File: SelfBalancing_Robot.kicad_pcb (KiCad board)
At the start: 2 copper layers, 58.4 x 53.3 mm, 10 parts, among them P1 CONN_01X08, P2 CONN_01X06, P3 CONN_01X02, P4 CONN_01X02, P5 CONN_01X02, U1 ArduinoNano, U2 L293D

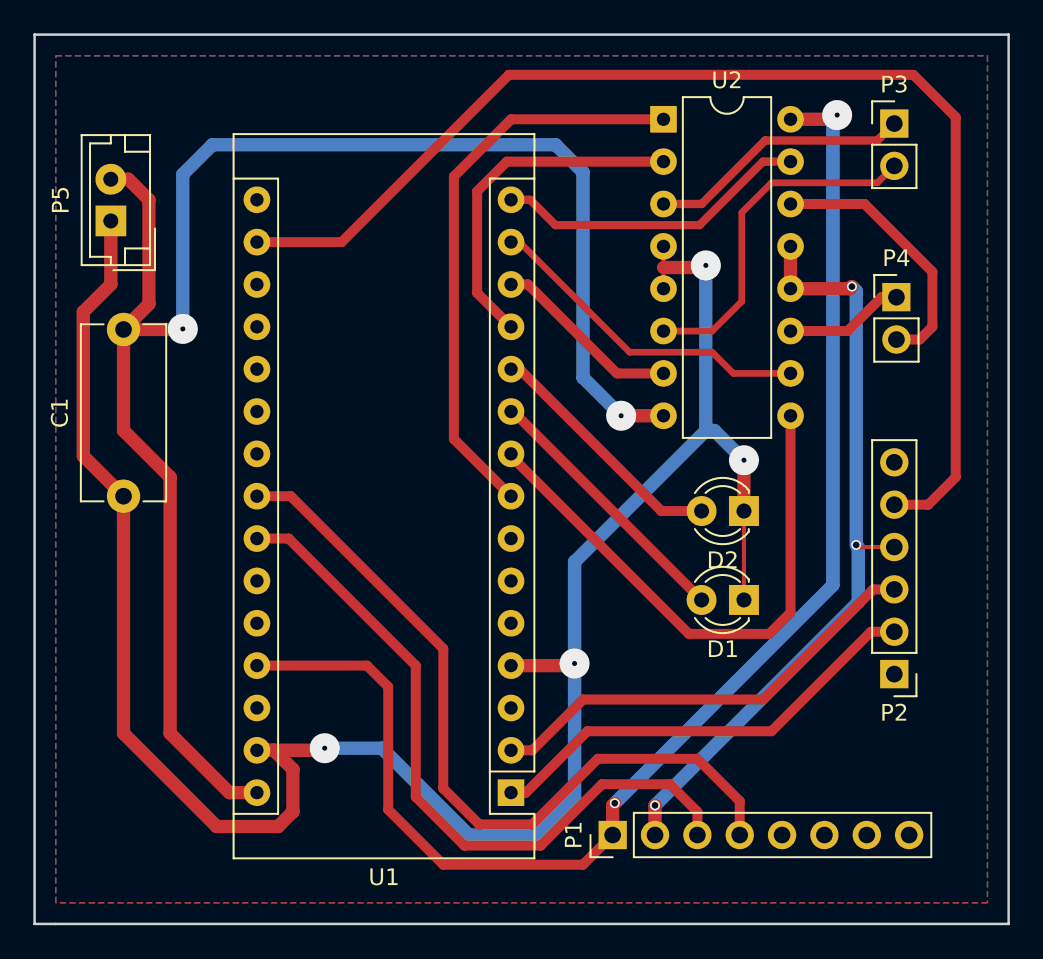
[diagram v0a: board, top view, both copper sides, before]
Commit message: +LED indicator resistors
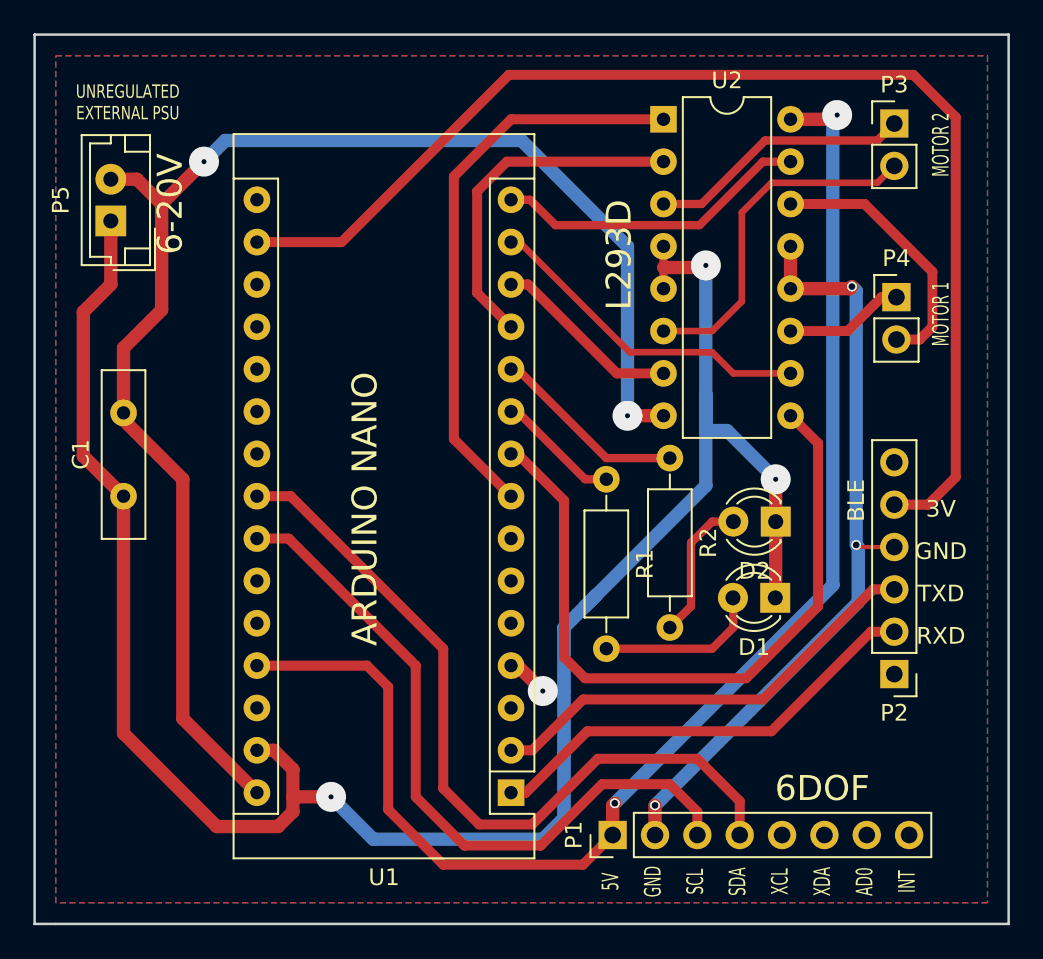
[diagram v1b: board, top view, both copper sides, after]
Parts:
- added R1: R, Resistors_ThroughHole:R_Axial_DIN0207_L6.3mm_D2.5mm_P10.16mm_Horizontal, F.Cu at (148.6, 97.8)
- added R2: R, Resistors_ThroughHole:R_Axial_DIN0207_L6.3mm_D2.5mm_P10.16mm_Horizontal, F.Cu at (152.4, 96.5)
- C1: footprint Capacitors_THT:C_Disc_D10.5mm_W5.0mm_P10.00mm -> Capacitors_THT:C_Disc_D10.0mm_W2.5mm_P5.00mm
- moved D2 2.01 mm to (158.8, 100.3)
- moved D1 1.88 mm to (158.7, 104.9)
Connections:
- U1 pad 10: Net-(D1-Pad2) -> Net-(R1-Pad1)
- U1 pad 11: Net-(D2-Pad2) -> Net-(R2-Pad1)
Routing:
- net Net-(R2-Pad1): track 0.00 -> 12.2 mm
- net /9V: track 99.6 -> 87.7 mm
- net /EN2: track 33.6 -> 43.5 mm
- net Net-(R1-Pad1): track 0.00 -> 7.53 mm
- net Net-(D1-Pad2): track 16.1 -> 9.42 mm
- net Net-(D2-Pad2): track 15.0 -> 8.67 mm
- net Net-(C1-Pad1): track 128.2 -> 132.0 mm
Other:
- board text added: "3V"
- board text added: "5V"
- board text added: "6-20V"
- board text added: "6DOF"
- board text added: "AD0"
- board text added: "ARDUINO NANO"
- board text added: "BLE"
- board text added: "GND"
- board text added: "INT"
- board text added: "L293D"
- board text added: "MOTOR 1"
- board text added: "MOTOR 2"
- board text added: "RXD"
- board text added: "SCL"
- board text added: "SDA"
- board text added: "TXD"
- board text added: "UNREGULATED EXTERNAL PSU"
- board text added: "XCL"
- board text added: "XDA"

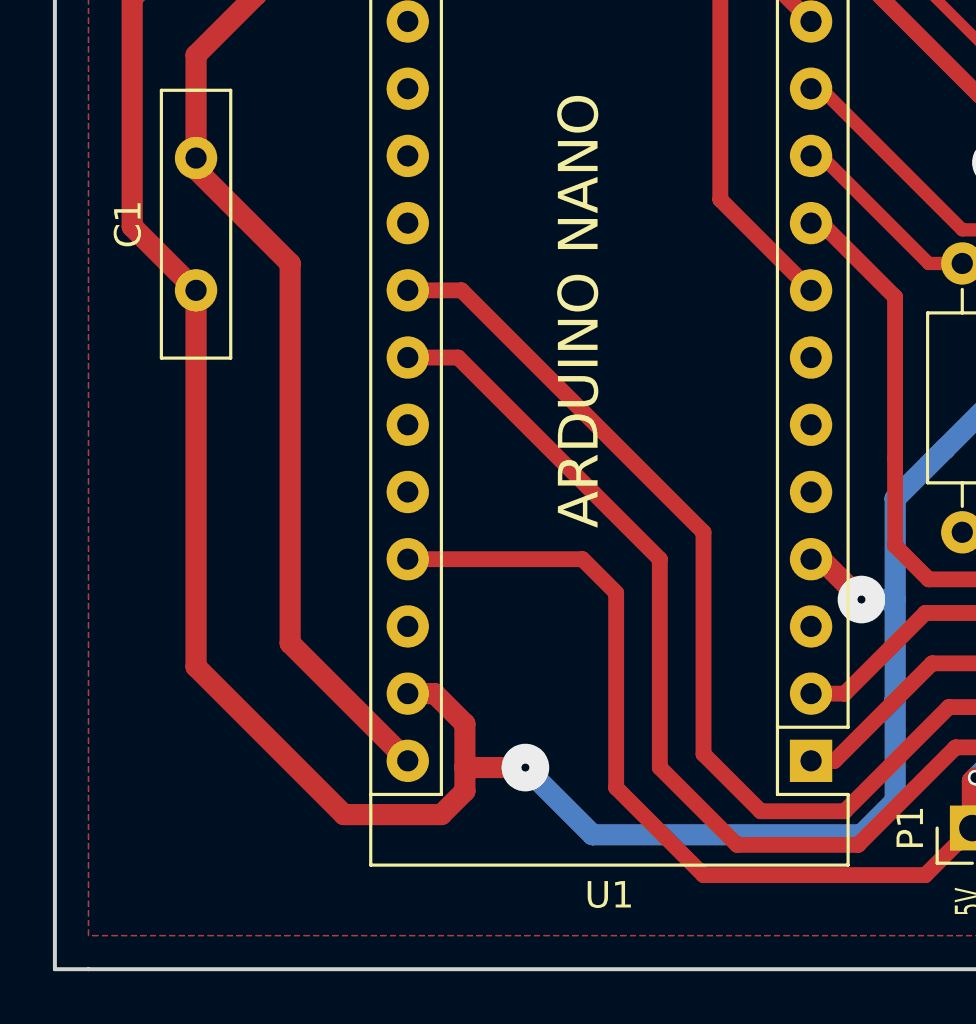
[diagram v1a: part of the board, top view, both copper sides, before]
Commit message: +servo connector pcb footprint
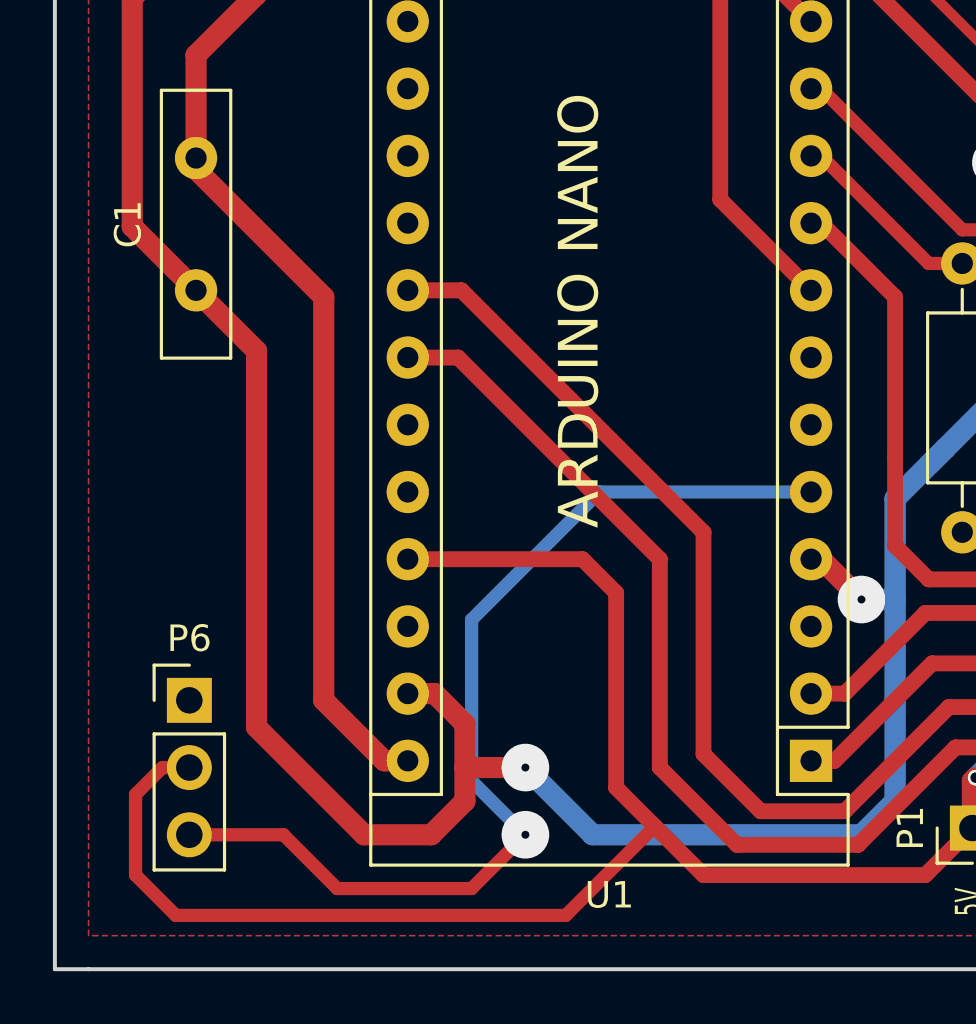
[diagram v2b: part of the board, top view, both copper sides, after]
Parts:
- added P6: CONN_01X03, Pin_Headers:Pin_Header_Straight_1x03_Pitch2.54mm, F.Cu at (119.4, 114.3)
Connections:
- U1 pad 5: (no net) -> /PWM
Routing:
- net /PWM: track 0.00 -> 38.2 mm, vias 0 -> 1
- net /5V: track 83.0 -> 110.1 mm
- net Net-(C1-Pad1): track 132.0 -> 132.9 mm
- net /9V: track 87.7 -> 88.2 mm

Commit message: *labels in silk
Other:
- board text added: "PWM"
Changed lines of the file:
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@@
     (area 114.224999 71.044999 172.795001 124.535001)
     (thickness 1.6)
-    (drawings 25)
+    (drawings 28)
     (tracks 208)
     (zones 0)
@@
     )
   )
+  (gr_text PWM (at 121.92 119.38) (layer F.SilkS)
+    (effects (font (size 1 0.6) (thickness 0.1)))
+  )
+  (gr_text 5V (at 121.92 116.84) (layer F.SilkS)
+    (effects (font (size 1 0.6) (thickness 0.1)))
+  )
+  (gr_text GND (at 121.92 114.3) (layer F.SilkS)
+    (effects (font (size 1 0.6) (thickness 0.1)))
+  )
   (gr_text "UNREGULATED\nEXTERNAL PSU" (at 119.888 75.184) (layer F.SilkS)

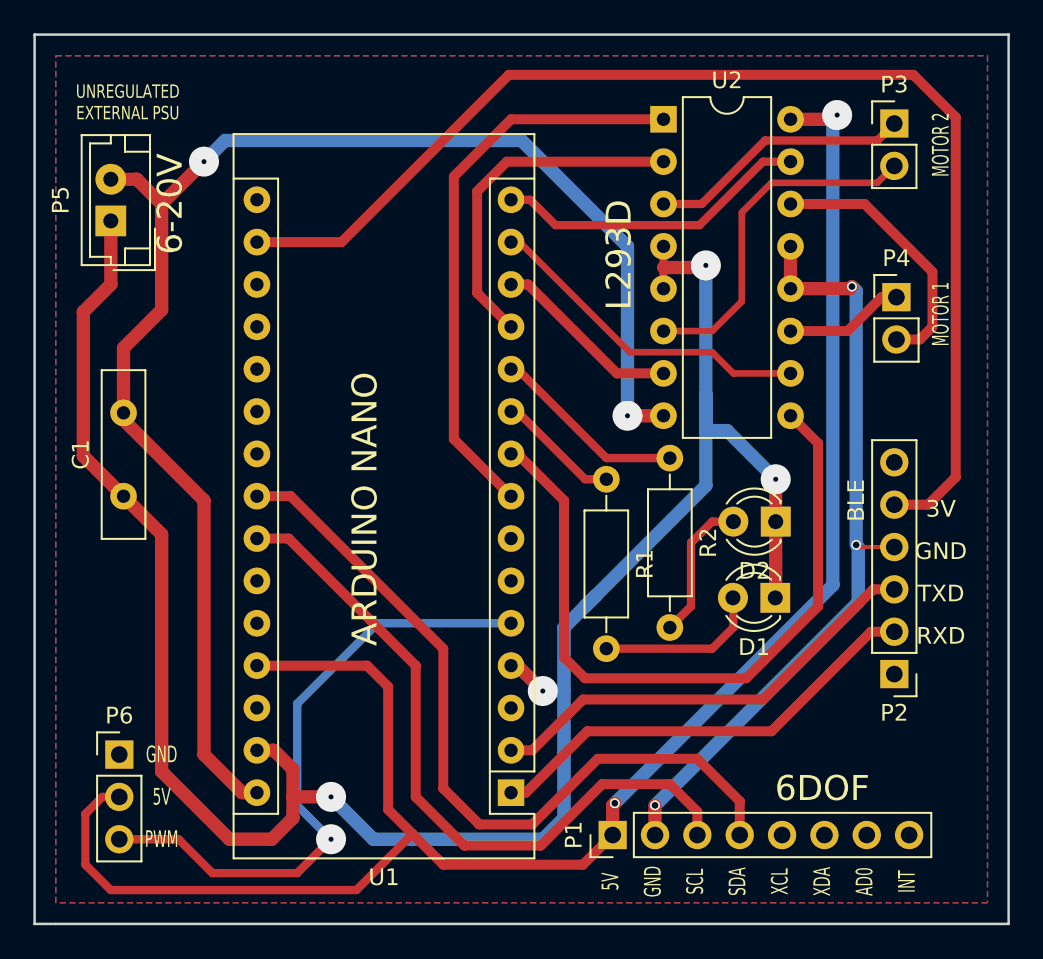
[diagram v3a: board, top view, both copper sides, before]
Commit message: +adding capacitors to L293D
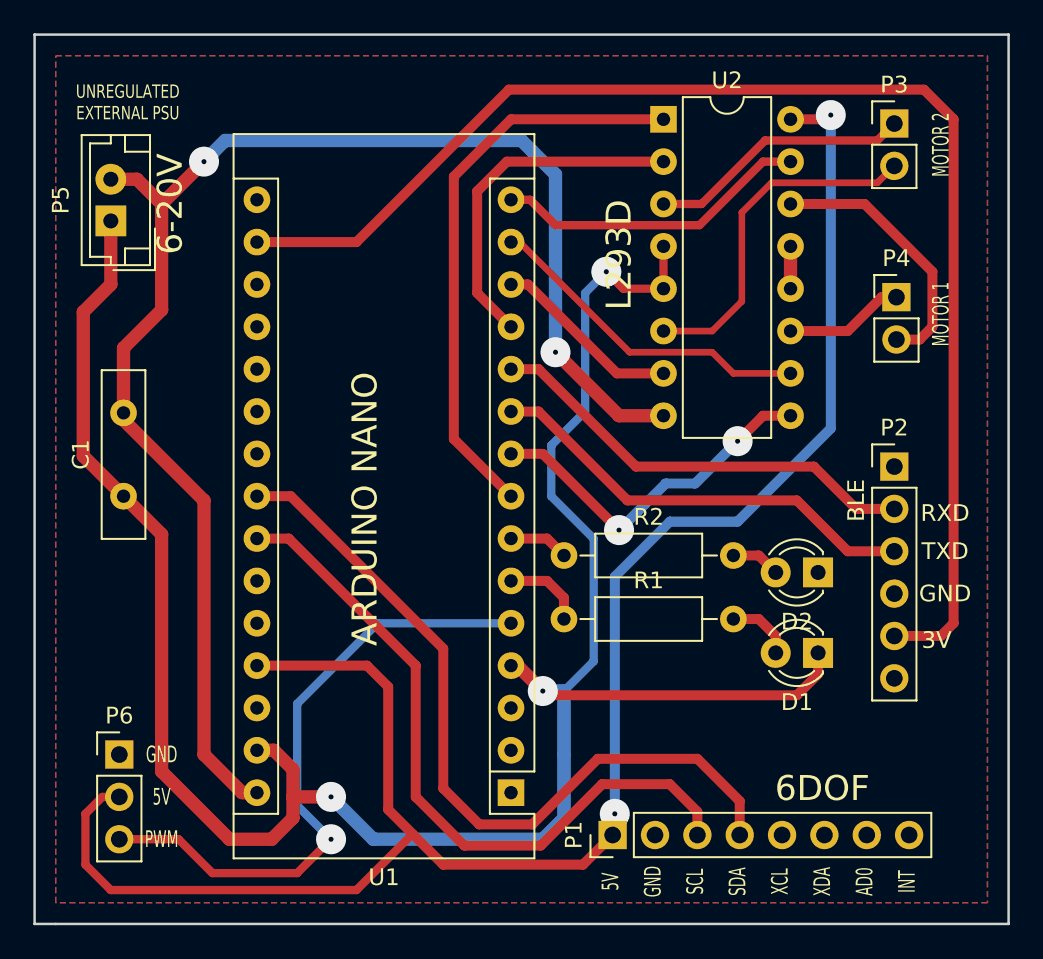
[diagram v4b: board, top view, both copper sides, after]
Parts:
- moved P2 12.4 mm to (165.9, 97.0), turned to 0 degrees
- moved R1 8.76 mm to (146.1, 106.2), turned to 0 degrees
- moved R2 8.63 mm to (146.1, 102.4), turned to 0 degrees
- moved D1 4.18 mm to (161.3, 108.2)
- moved D2 3.97 mm to (161.3, 103.4)
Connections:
- U1 pad 1: /RXD -> (no net)
- U1 pad 10: Net-(R1-Pad1) -> /TXD
- U1 pad 11: Net-(R2-Pad1) -> /RXD
- U1 pad 2: /TXD -> (no net)
- U1 pad 6: (no net) -> Net-(R1-Pad1)
- U1 pad 7: (no net) -> Net-(R2-Pad1)
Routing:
- net /GND: track 46.7 -> 2.54 mm, vias 3 -> 0
- net /EN2: track 43.5 -> 22.0 mm, vias 0 -> 2
- net Net-(R2-Pad1): track 12.2 -> 3.60 mm
- net /3V3: track 73.1 -> 80.4 mm
- net Net-(D2-Pad2): track 8.67 -> 2.96 mm
- net Net-(C1-Pad1): track 132.9 -> 138.3 mm, vias 4 -> 3
- net Net-(D1-Pad2): track 9.42 -> 3.98 mm
- net Net-(R1-Pad1): track 7.53 -> 4.87 mm
- net /5V: track 110.1 -> 112.0 mm
